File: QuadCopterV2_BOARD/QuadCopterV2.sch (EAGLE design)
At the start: 10 parts, among them IC1 EK-TM4C123GXLP, U1 GY-63MS5611, U2 GY-521MPU6050, U3 GY-63MS5611

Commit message: Eagle board design in process
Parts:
- removed U$1: SIM800L, SIM800L:SIM800L
- added U$7: SIM800L, SIM800L:SIM800L
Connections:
- removed net N$27: U$1.VDD
- removed net N$28: U$1.TXD
- removed net N$30: U$1.RST
- removed net N$31: U$1.RXD
- new net 5V1: U$2.VCC
- new net N$1: U$7.VDD
- new net N$15: U$7.RXD
- new net N$6: U$7.TXD
- new net N$7: U$7.RST
- net 5V0: now also U$7.5V; no longer U$1.5V, U$2.VCC
- net GND: now also U$7.GND; no longer U$1.GND
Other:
- note added: "Author: Fernando Fontes"
- note added: "Barometer module. This module will be the master piece for the altitude lock mode. Used for locking altitude and to other things."
- note added: "Bluethooth module. This module will be used for remote controling the quadcopter. The controler will be the same of the version 1."
- note added: "ESP-01 Wifi module. The purpose of this module is not known for shure yet. Maybe it can be used to publish some variables to the internet when it reaches some know network, or maybe can be used for OTA programming. Can be also set to listen to some commands and act accordently."
- note added: "GPS module. This module will help in the head lock procedure, and be useful for getting the geographic coordinates, that can be used for later automatization."
- note added: "Gyroscope module. Used for the stabilization procedure. Has an internal accelerometer too."
- note added: "HC-12 RF modude. This module as a long working range. Around 1 km. So, it can be used for extending the range of the controller. It's needed of course some sort of trasmitter that uses the same module."
- note added: "HC-SR04. Ultra-Sonic sensor. Common used in distance measuring procedures. In this project, it will be also used to help in the landing, measuring the distance to the ground and also detecting the presence of obstacles."
- note added: "Main power board. Receives as input 12.6V from a Lithium-ion battery, and distributes the power to the ESC's modules and also for the restant parts of the controller board."
- note added: "Quadcopter Controller Board. Composed by a Texas EK-TM4C."
- note added: "SIM800L GSM board. Used for transmitting controls at distance. Can be used to transmit position coordinates, and also to receive some destination coordinates."
- note removed: "Quadcopter Controller Board. Author: Fernando Fontes"

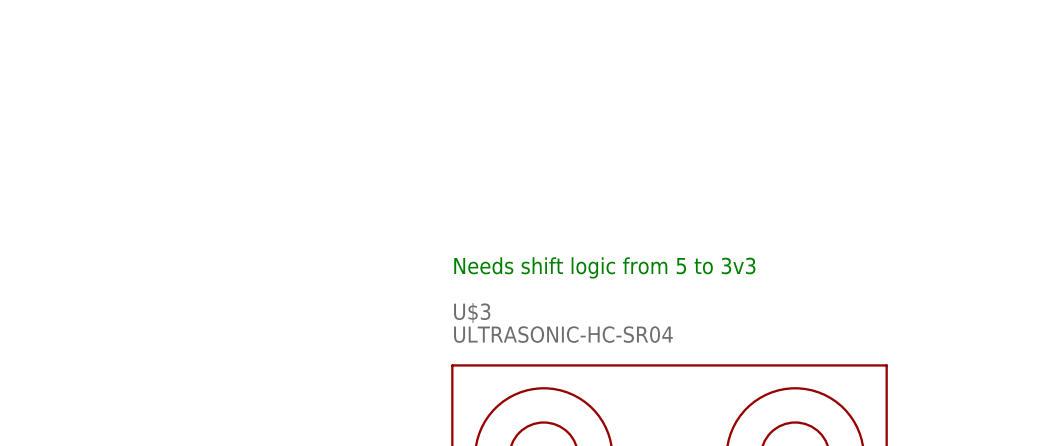
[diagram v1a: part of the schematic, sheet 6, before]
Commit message: added modifications to eagle board, and to the mpu-6050 code
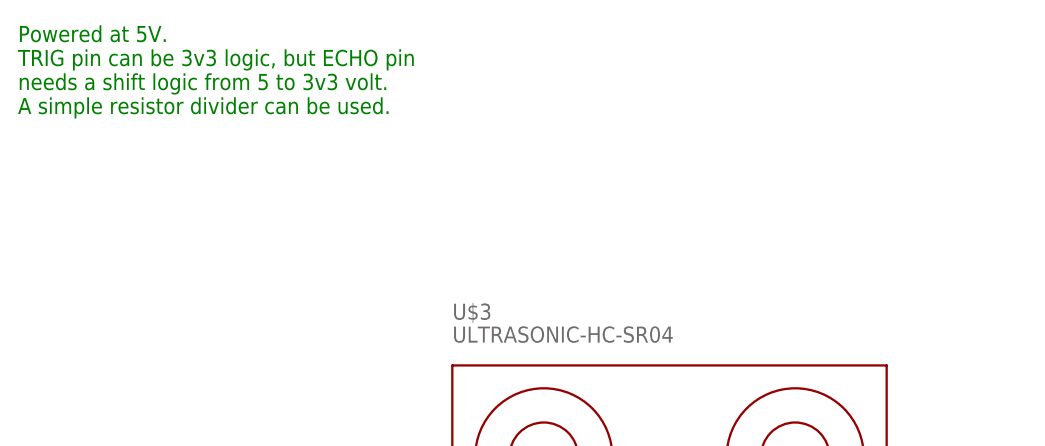
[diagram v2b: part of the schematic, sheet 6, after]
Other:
- note added: "No need for shift logic levels. RX and TX lines are 3V3 logic."
- note added: "Powered at 5V, but RX and TX lines are 3v3 logic. No need for shift logic then."
- note added: "Powered at 5V. TRIG pin can be 3v3 logic, but ECHO pin needs a shift logic from 5 to 3v3 volt. A simple resistor divider can be used."
- note added: "Powered at 5v. However, SCL and SDA lines are 3v3 pulled up. So no need for shift logic converter."
- note removed: "Connects to 3V3"
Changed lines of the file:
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@@
 <description>ESP-01 WIFI BOARD</description>
 <plain>
-<text x="66.04" y="38.1" size="1.778" layer="91">Connects to 3V3</text>
+<text x="-5.08" y="96.52" size="1.778" layer="91">No need for shift logic levels.
+RX and TX lines are 3V3 logic.</text>
 <text x="127" y="7.62" size="1.778" layer="91">Author: Fernando Fontes</text>
 <text x="66.04" y="-7.62" size="1.778" layer="91">ESP-01 Wifi module. The purpose of this
@@
 <description>HC-05 BLUETOOTH MODULE</description>
 <plain>
-<text x="81.28" y="50.8" size="1.778" layer="91">Needs shift logic from 5 to 3v3</text>
+<text x="20.32" y="76.2" size="1.778" layer="91">Powered at 5V, but RX and TX lines are 3v3 logic.
+No need for shift logic then.</text>
 <text x="147.32" y="-15.24" size="1.778" layer="91">Author: Fernando Fontes</text>
 <text x="91.44" y="-30.48" size="1.778" layer="91">Bluethooth module. This module
@@
 <description>HC-SR04 ULTRA-SOUND MODULE</description>
 <plain>
-<text x="63.5" y="73.66" size="1.778" layer="91">Needs shift logic from 5 to 3v3</text>
+<text x="15.24" y="91.44" size="1.778" layer="91">Powered at 5V.
+TRIG pin can be 3v3 logic, but ECHO pin
+needs a shift logic from 5 to 3v3 volt.
+A simple resistor divider can be used.</text>
 <text x="142.24" y="2.54" size="1.778" layer="91">Author: Fernando Fontes</text>
 <text x="83.82" y="-12.7" size="1.778" layer="91">HC-SR04. Ultra-Sonic sensor. Common
@@
 <text x="73.66" y="-2.54" size="1.778" layer="91">Gyroscope module. Used for the stabilization
 procedure. Has an internal accelerometer too.</text>
-</plain>
-<instances>
+<text x="2.54" y="104.14" size="1.778" layer="91">Powered at 5v. However, SCL and SDA lines are 3v3 pulled up.
+So no need for shift logic converter.</text>
+</plain>
+<instances>

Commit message: news modifications on designed board
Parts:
- added C1, C2, C3, C4, C5, C6: C4.7U-SMD, smd-rlc:C4.7U-SMD
- added R1, R2: RSMD, smd-resistor:RSMD
- added R3, R4, R5: RSMD, smd-rlc:RSMD
- added U$1: SIM800L, SIM800L:SIM800L
- added U10, U7, U8, U9: ESC-30AMS5611, ESC-HW30A:ESC-30AMS5611
- added U4, U5, U6: MCP1825S-3302E/DBP1, MCP1825S-3302E_DB:MCP1825S-3302E/DBP1
- U$3: value ULTRASONIC-HC-SR04 -> ULTRASONIC-HC-SR04#P; device diy-modules:ULTRASONIC-HC-SR04 -> diy-modules:ULTRASONIC-HC-SR04#P
- U$7: value SIM800L -> XT60; device SIM800L:SIM800L -> XT60:XT60
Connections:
- net A0 renamed PE3
- net ENABLE_4 renamed PB3
- net PA_3 renamed PA3
- net PA_4 renamed PA4
- net SPI_MISO_3 renamed PD2
- net U7_RX renamed PE0
- removed net 5V1: U$2.VCC
- removed net ENABLE_0: IC1.PB4
- removed net ENABLE_1: IC1.PA5
- removed net ENABLE_2: IC1.PC5
- removed net ENABLE_3: IC1.PC4
- removed net ENABLE_5: IC1.PB6
- removed net ENABLE_6: IC1.PB7
- removed net N$10: U3.SCL
- removed net N$11: U3.SDA
- removed net N$12: U$5.SET
- removed net N$13: U$5.TX
- removed net N$14: U$5.RX
- removed net N$15: U$7.RXD
- removed net N$19: U$2.UTXD
- removed net N$2: U$4.EN
- removed net N$21: U$2.CH_PD
- removed net N$23: U$2.RST
- removed net N$24: U$2.URXD
- removed net N$3: U$4.TX
- removed net N$33: U$3.TRIG
- removed net N$38: U1.SCL
- removed net N$39: U1.SDA
- removed net N$4: U$4.RX
- removed net N$43: U2.SCL
- removed net N$44: U2.SDA
- removed net N$5: U$4.STATE
- removed net N$6: U$7.TXD
- removed net N$7: U$7.RST
- removed net N$8: U3.UART_TX
- removed net N$9: U3.UART_RX
- removed net PA_2: IC1.PA2
- removed net PB_2: IC1.PB2
- removed net SPI_CS_3: IC1.PD1
- removed net SPI_MOSI_3: IC1.PD3
- removed net SPI_SCK_3: IC1.PD0
- removed net U7_TX: IC1.PE1
- new net 3V3_ESP: C4.2, U$2.CH_PD, U$2.VCC, U4.VOUT
- new net 3V3_HC12: C2.2, U$5.VCC, U6.VOUT
- new net 3V3_MS5611: C6.2, U$1.VDD, U1.VCC, U5.VOUT
- new net PA2: IC1.PA2, U$2.RST
- new net PA5: IC1.PA5, U$4.EN
- new net PB2: IC1.PB2, U$1.RST
- new net PB4: IC1.PB4, U$4.STATE
- new net PB6: IC1.PB6, U9.PWM
- new net PB7: IC1.PB7, U10.PWM
- new net PD0: IC1.PD0, U7.PWM
- new net PD1: IC1.PD1, U8.PWM
- new net PD3: IC1.PD3, R3.1, R4.1
- new net PE1: IC1.PE1, U$3.TRIG
- new net U4_RX: IC1.PC4, U$1.SIM_TXD
- new net U4_TX: IC1.PC5, U$1.SIM_RXD
- net 5V0: now also C1.1, C3.2, C5.1, R5.2, U$1.PW_5V, U4.VIN, U5.VIN, U6.VIN; no longer IC1.+5V, U$5.VCC, U$7.5V, U1.VCC
- net GND: now also C1.2, C2.1, C3.1, C4.1, C5.2, C6.1, R2.1, R4.2, U$1.GND, U$1.PW_GND, U10.GND, U4.GND_(TAB), U5.GND_(TAB), U6.GND_(TAB), U7.GND, U8.GND, U9.GND; no longer U$7.GND
- net I2C_SCL_1: now also U1.SCL, U2.SCL, U3.SCL
- net I2C_SDA_1: now also U1.SDA, U2.SDA, U3.SDA
- net N$1: now also IC1.+5V, R5.1; no longer U$7.VDD
- net N$34: now also R1.1
- net PB5: now also U$5.SET
- net PE2: now also R1.2, R2.2
- net U1_RX: now also U$5.TX
- net U1_TX: now also U$5.RX
- net U2_RX: now also U3.UART_TX
- net U2_TX: now also U3.UART_RX
- net U3_RX: now also U$2.UTXD
- net U3_TX: now also U$2.URXD
- net U5_RX: now also U$4.TX
- net U5_TX: now also U$4.RX
- net VBAT+: now also R3.2, U$7.VCC
- net VBAT-: now also U$7.GND
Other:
- note removed: "Needs shift logic from 5 to 3v3"

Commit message: final version of quadcopter board
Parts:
- removed R5: RSMD, smd-rlc:RSMD
- added R6: RSMD, smd-rlc:RSMD
- R1: value RSMD -> 1k7; device smd-resistor:RSMD -> smd-rlc:RSMD
- R2: value RSMD -> 3K3; device smd-resistor:RSMD -> smd-rlc:RSMD
- R3: value RSMD -> 11k7
- R4: value RSMD -> 3k3
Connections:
- removed net GND2: IC1.GND2
- removed net N$17: U$5.ANT
- net 5V0: now also R6.2; no longer R5.2
- net GND: now also IC1.GND2
- net N$1: now also R6.1; no longer R5.1
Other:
- note added: "ANT"
